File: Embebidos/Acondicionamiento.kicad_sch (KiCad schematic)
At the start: 21 parts, among them IC1 ESP32-WROVER-B__8MB_, SW1 SW_Reset, SW2 SW_Boot

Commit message: LDR_69Errores
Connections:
- net LDR_IN: now reaches IC1.7 (IO35)
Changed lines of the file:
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@@
     (effects (font (size 1.27 1.27)) (justify left))
+  )
+  (hierarchical_label "LDR_IN" (shape input) (at 114.3 83.82 180)
+    (effects (font (size 1.27 1.27)) (justify right))
   )
   (hierarchical_label "RXSIM" (shape bidirectional) (at 186.69 107.95 0)

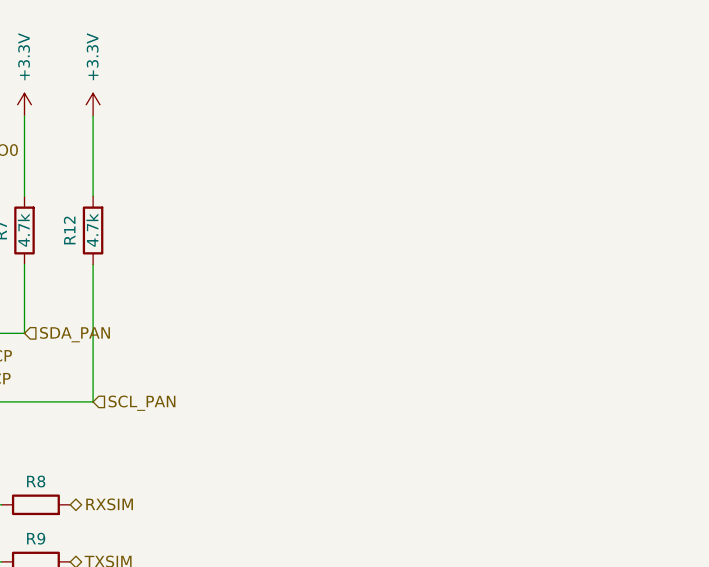
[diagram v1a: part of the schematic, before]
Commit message: conectoresRFySIM
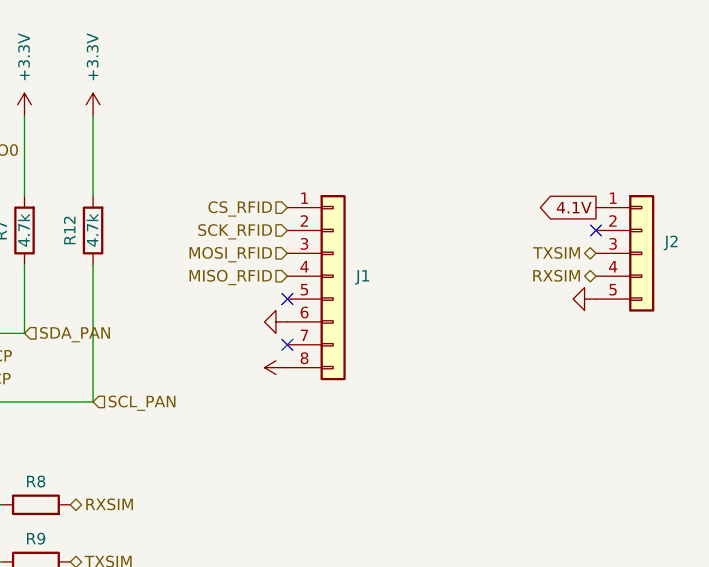
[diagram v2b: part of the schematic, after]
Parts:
- added J1: (no value), symbol Connector_Generic:Conn_01x08
- added J2: (no value), symbol Connector_Generic:Conn_01x05
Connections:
- net +3.3V: now also J1.8 (Pin_8)
- net CS_RFID: now also J1.1 (Pin_1)
- net GND: now also J1.6 (Pin_6), J2.5 (Pin_5)
- net MISO_RFID: now also J1.4 (Pin_4)
- net MOSI_RFID: now also J1.3 (Pin_3)
- net RXSIM: now also J2.4 (Pin_4)
- net SCK_RFID: now also J1.2 (Pin_2)
- net TXSIM: now also J2.3 (Pin_3)
- new net 4.1V: J2.1 (Pin_1)
- no-connect marks 19 -> 22

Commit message: Mosfet Luces
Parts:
- J1: value (none) -> Conn_01x08
- J2: value (none) -> Conn_01x05
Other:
- moved on the sheet: J1, J2
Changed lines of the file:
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@@
   (no_connect (at 152.4 76.2))
   (no_connect (at 152.4 86.36))
-  (no_connect (at 245.11 77.47))
+  (no_connect (at 251.46 24.13))
   (no_connect (at 152.4 104.14))
   (no_connect (at 152.4 114.3))
   (no_connect (at 152.4 124.46))
-  (no_connect (at 210.82 85.09))
-  (no_connect (at 210.82 90.17))
+  (no_connect (at 251.46 58.42))
+  (no_connect (at 251.46 63.5))
   (wire (pts (xy 68.58 80.01) (xy 68.58 82.55))
     (stroke (width 0) (type default) (color 0 0 0 0))
@@
     (effects (font (size 1.27 1.27)) (justify right bottom))
   )
-  (global_label "4.1V" (shape output) (at 245.11 74.93 180) (fields_autoplaced)
-    (effects (font (size 1.27 1.27)) (justify right))
-    (property "Intersheet References" "${INTERSHEET_REFS}" (id 0) (at 238.5845 74.8506 0)
+  (global_label "4.1V" (shape output) (at 251.46 21.59 180) (fields_autoplaced)
+    (effects (font (size 1.27 1.27)) (justify right))
+    (property "Intersheet References" "${INTERSHEET_REFS}" (id 0) (at 244.9345 21.5106 0)
       (effects (font (size 1.27 1.27)) (justify right) hide)
     )
@@
     (effects (font (size 1.27 1.27)) (justify right))
   )
-  (hierarchical_label "MOSI_RFID" (shape input) (at 210.82 80.01 180)
+  (hierarchical_label "MOSI_RFID" (shape input) (at 251.46 53.34 180)
     (effects (font (size 1.27 1.27)) (justify right))
   )
@@
     (effects (font (size 1.27 1.27)) (justify left))
   )
-  (hierarchical_label "TXSIM" (shape bidirectional) (at 245.11 80.01 180)
+  (hierarchical_label "TXSIM" (shape bidirectional) (at 251.46 26.67 180)
     (effects (font (size 1.27 1.27)) (justify right))
   )
@@
     (effects (font (size 1.27 1.27)) (justify right))
   )
-  (hierarchical_label "MISO_RFID" (shape input) (at 210.82 82.55 180)
+  (hierarchical_label "MISO_RFID" (shape input) (at 251.46 55.88 180)
     (effects (font (size 1.27 1.27)) (justify right))
   )
@@
     (effects (font (size 1.27 1.27)) (justify right))
   )
-  (hierarchical_label "RXSIM" (shape bidirectional) (at 245.11 82.55 180)
+  (hierarchical_label "RXSIM" (shape bidirectional) (at 251.46 29.21 180)
     (effects (font (size 1.27 1.27)) (justify right))
   )
@@
     (effects (font (size 1.27 1.27)) (justify left))
   )
-  (hierarchical_label "CS_RFID" (shape input) (at 210.82 74.93 180)
-    (effects (font (size 1.27 1.27)) (justify right))
-  )
-  (hierarchical_label "SCK_RFID" (shape input) (at 210.82 77.47 180)
+  (hierarchical_label "CS_RFID" (shape input) (at 251.46 48.26 180)
+    (effects (font (size 1.27 1.27)) (justify right))
+  )
+  (hierarchical_label "SCK_RFID" (shape input) (at 251.46 50.8 180)
     (effects (font (size 1.27 1.27)) (justify right))
   )
@@
     (effects (font (size 1.27 1.27)) (justify left))
   )
-  (symbol (lib_id "Connector_Generic:Conn_01x08") (at 215.9 82.55 0) (unit 1)
-    (in_bom yes) (on_board yes) (fields_autoplaced)
-    (property "Reference" "J1" (id 0) (at 218.44 82.5499 0)
-      (effects (font (size 1.27 1.27)) (justify left))
-    )
-    (property "Value" "" (id 1) (at 218.44 85.0899 0)
-      (effects (font (size 1.27 1.27)) (justify left))
-    )
-    (property "Footprint" "" (id 2) (at 215.9 82.55 0)
-      (effects (font (size 1.27 1.27)) hide)
-    )
-    (property "Datasheet" "~" (id 3) (at 215.9 82.55 0)
+  (symbol (lib_id "Connector_Generic:Conn_01x08") (at 256.54 55.88 0) (unit 1)
+    (in_bom yes) (on_board yes) (fields_autoplaced)
+    (property "Reference" "J1" (id 0) (at 259.08 55.8799 0)
+      (effects (font (size 1.27 1.27)) (justify left))
+    )
+    (property "Value" "Conn_01x08" (id 1) (at 259.08 58.4199 0)
+      (effects (font (size 1.27 1.27)) (justify left))
+    )
+    (property "Footprint" "" (id 2) (at 256.54 55.88 0)
+      (effects (font (size 1.27 1.27)) hide)
+    )
+    (property "Datasheet" "~" (id 3) (at 256.54 55.88 0)
       (effects (font (size 1.27 1.27)) hide)
     )
@@
     (pin "2")
   )
-  (symbol (lib_id "Connector_Generic:Conn_01x05") (at 250.19 80.01 0) (unit 1)
-    (in_bom yes) (on_board yes) (fields_autoplaced)
-    (property "Reference" "J2" (id 0) (at 252.73 78.7399 0)
-      (effects (font (size 1.27 1.27)) (justify left))
-    )
-    (property "Value" "" (id 1) (at 252.73 81.2799 0)
-      (effects (font (size 1.27 1.27)) (justify left))
-    )
-    (property "Footprint" "" (id 2) (at 250.19 80.01 0)
-      (effects (font (size 1.27 1.27)) hide)
-    )
-    (property "Datasheet" "~" (id 3) (at 250.19 80.01 0)
+  (symbol (lib_id "Connector_Generic:Conn_01x05") (at 256.54 26.67 0) (unit 1)
+    (in_bom yes) (on_board yes) (fields_autoplaced)
+    (property "Reference" "J2" (id 0) (at 259.08 25.3999 0)
+      (effects (font (size 1.27 1.27)) (justify left))
+    )
+    (property "Value" "Conn_01x05" (id 1) (at 259.08 27.9399 0)
+      (effects (font (size 1.27 1.27)) (justify left))
+    )
+    (property "Footprint" "" (id 2) (at 256.54 26.67 0)
+      (effects (font (size 1.27 1.27)) hide)
+    )
+    (property "Datasheet" "~" (id 3) (at 256.54 26.67 0)
       (effects (font (size 1.27 1.27)) hide)
     )
@@
     (pin "1")
   )
-  (symbol (lib_id "power:+3.3V") (at 210.82 92.71 90) (unit 1)
-    (in_bom yes) (on_board yes) (fields_autoplaced)
-    (property "Reference" "#PWR?" (id 0) (at 214.63 92.71 0)
-      (effects (font (size 1.27 1.27)) hide)
-    )
-    (property "Value" "" (id 1) (at 207.01 92.7099 90)
-      (effects (font (size 1.27 1.27)) (justify left))
-    )
-    (property "Footprint" "" (id 2) (at 210.82 92.71 0)
-      (effects (font (size 1.27 1.27)) hide)
-    )
-    (property "Datasheet" "" (id 3) (at 210.82 92.71 0)
+  (symbol (lib_id "power:+3.3V") (at 251.46 66.04 90) (unit 1)
+    (in_bom yes) (on_board yes) (fields_autoplaced)
+    (property "Reference" "#PWR?" (id 0) (at 255.27 66.04 0)
+      (effects (font (size 1.27 1.27)) hide)
+    )
+    (property "Value" "+3.3V" (id 1) (at 247.65 66.0399 90)
+      (effects (font (size 1.27 1.27)) (justify left))
+    )
+    (property "Footprint" "" (id 2) (at 251.46 66.04 0)
+      (effects (font (size 1.27 1.27)) hide)
+    )
+    (property "Datasheet" "" (id 3) (at 251.46 66.04 0)
       (effects (font (size 1.27 1.27)) hide)
     )
@@
     (pin "1")
   )
-  (symbol (lib_id "power:GND") (at 210.82 87.63 270) (unit 1)
-    (in_bom yes) (on_board yes) (fields_autoplaced)
-    (property "Reference" "#PWR?" (id 0) (at 204.47 87.63 0)
-      (effects (font (size 1.27 1.27)) hide)
-    )
-    (property "Value" "" (id 1) (at 207.01 87.6299 90)
+  (symbol (lib_id "power:GND") (at 251.46 60.96 270) (unit 1)
+    (in_bom yes) (on_board yes) (fields_autoplaced)
+    (property "Reference" "#PWR?" (id 0) (at 245.11 60.96 0)
+      (effects (font (size 1.27 1.27)) hide)
+    )
+    (property "Value" "GND" (id 1) (at 247.65 60.9599 90)
       (effects (font (size 1.27 1.27)) (justify right))
     )
-    (property "Footprint" "" (id 2) (at 210.82 87.63 0)
-      (effects (font (size 1.27 1.27)) hide)
-    )
-    (property "Datasheet" "" (id 3) (at 210.82 87.63 0)
+    (property "Footprint" "" (id 2) (at 251.46 60.96 0)
+      (effects (font (size 1.27 1.27)) hide)
+    )
+    (property "Datasheet" "" (id 3) (at 251.46 60.96 0)
       (effects (font (size 1.27 1.27)) hide)
     )
@@
     (pin "1")
   )
-  (symbol (lib_id "power:GND") (at 245.11 85.09 270) (unit 1)
-    (in_bom yes) (on_board yes) (fields_autoplaced)
-    (property "Reference" "#PWR?" (id 0) (at 238.76 85.09 0)
-      (effects (font (size 1.27 1.27)) hide)
-    )
-    (property "Value" "" (id 1) (at 241.3 85.0899 90)
+  (symbol (lib_id "power:GND") (at 251.46 31.75 270) (unit 1)
+    (in_bom yes) (on_board yes) (fields_autoplaced)
+    (property "Reference" "#PWR?" (id 0) (at 245.11 31.75 0)
+      (effects (font (size 1.27 1.27)) hide)
+    )
+    (property "Value" "GND" (id 1) (at 247.65 31.7499 90)
       (effects (font (size 1.27 1.27)) (justify right))
     )
-    (property "Footprint" "" (id 2) (at 245.11 85.09 0)
-      (effects (font (size 1.27 1.27)) hide)
-    )
-    (property "Datasheet" "" (id 3) (at 245.11 85.09 0)
-      (effects (font (size 1.27 1.27)) hide)
-    )
+    (property "Footprint" "" (id 2) (at 251.46 31.75 0)
+      (effects (font (size 1.27 1.27)) hide)
+    )
+    (property "Datasheet" "" (id 3) (at 251.46 31.75 0)
+      (effects (font (size 1.27 1.27)) hide)
+    )

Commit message: COnecxion
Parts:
- R1: value ~ -> 470
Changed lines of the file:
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@@
     (in_bom yes) (on_board yes)
     (property "Reference" "R1" (id 0) (at 59.69 78.74 90))
-    (property "Value" "~" (id 1) (at 57.15 78.74 90))
+    (property "Value" "470" (id 1) (at 57.15 78.74 90))
     (property "Footprint" "" (id 2) (at 55.372 78.74 90)
       (effects (font (size 1.27 1.27)) hide)

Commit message: transistores traseros
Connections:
- net CTR 5V Inf: no longer names the net of IC1.14 (IO12)
- net CTR 5V LEDS renamed ctr_trasero
- net CTR_LED_delantero renamed ctr_led_delantero
- no-connect marks 22 -> 23
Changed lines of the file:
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@@
   (no_connect (at 152.4 119.38))
   (no_connect (at 152.4 106.68))
+  (no_connect (at 114.3 101.6))
   (no_connect (at 152.4 73.66))
   (no_connect (at 152.4 76.2))
@@
     (effects (font (size 1.27 1.27)) (justify left))
   )
-  (hierarchical_label "CTR 5V LEDS" (shape output) (at 152.4 71.12 0)
+  (hierarchical_label "ctr_trasero" (shape output) (at 152.4 71.12 0)
     (effects (font (size 1.27 1.27)) (justify left))
   )
@@
     (effects (font (size 1.27 1.27)) (justify left))
   )
-  (hierarchical_label "CTR_LED_delantero" (shape output) (at 114.3 127 180)
+  (hierarchical_label "ctr_led_delantero" (shape output) (at 114.3 127 180)
     (effects (font (size 1.27 1.27)) (justify right))
   )
@@
     (effects (font (size 1.27 1.27)) (justify right))
   )
-  (hierarchical_label "CTR 5V Inf" (shape output) (at 114.3 101.6 180)
-    (effects (font (size 1.27 1.27)) (justify right))
-  )

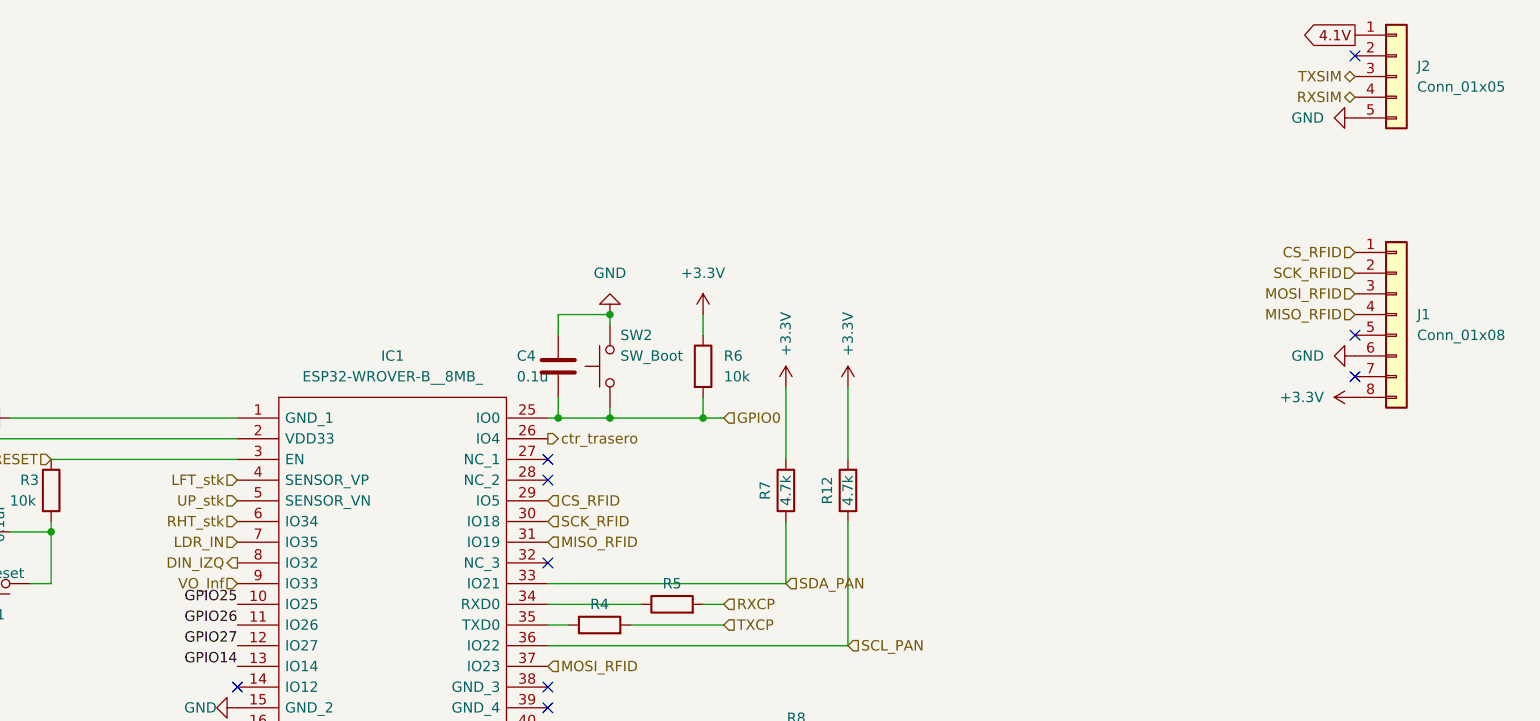
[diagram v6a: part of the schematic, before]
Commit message: Cambio de anotacion y Vcc ldr
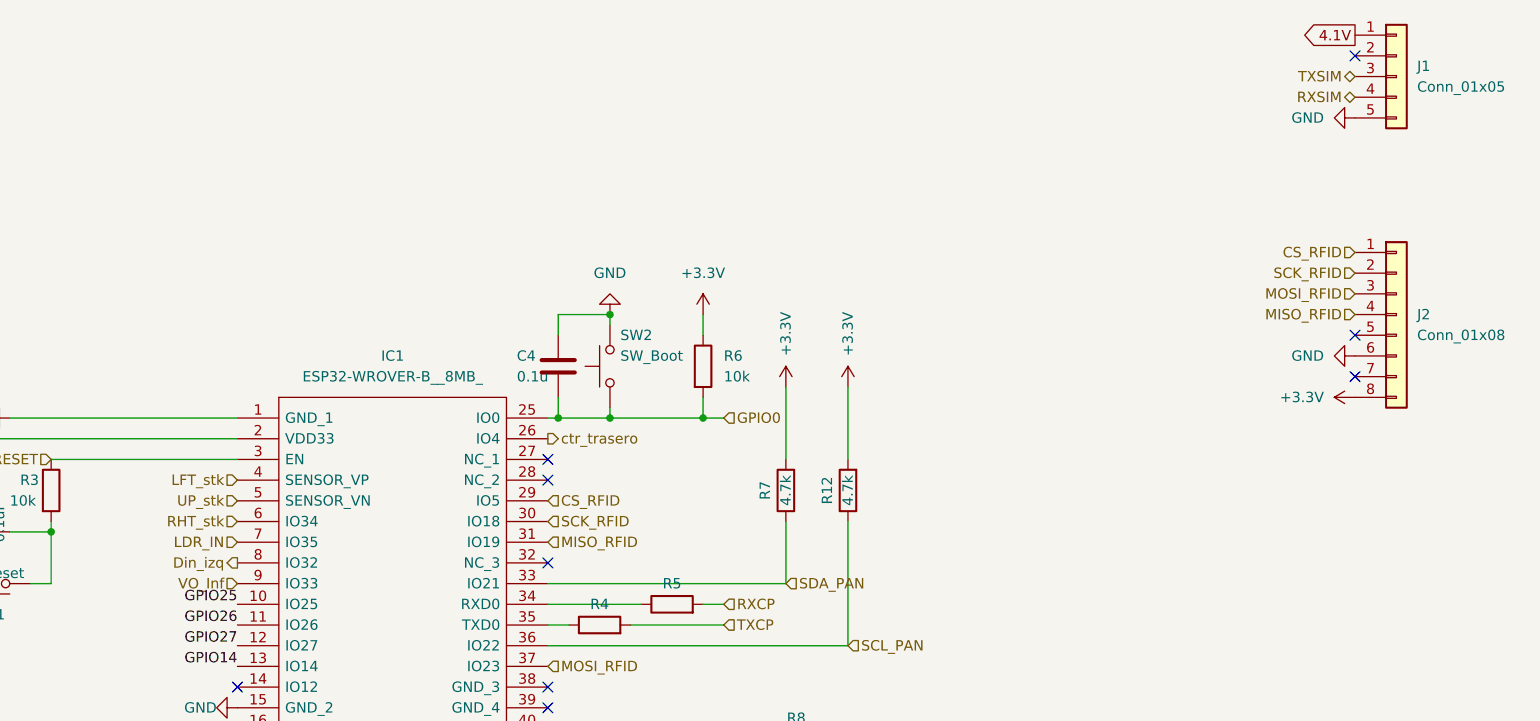
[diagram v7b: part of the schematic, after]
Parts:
- renumbered J2 to J1, J1 to J2
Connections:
- net DIN_IZQ renamed Din_izq
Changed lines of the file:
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@@
     (effects (font (size 1.27 1.27)) (justify right))
   )
-  (hierarchical_label "DIN_IZQ" (shape output) (at 114.3 86.36 180)
+  (hierarchical_label "Din_izq" (shape output) (at 114.3 86.36 180)
     (effects (font (size 1.27 1.27)) (justify right))
   )
@@
   (symbol (lib_id "Connector_Generic:Conn_01x08") (at 256.54 55.88 0) (unit 1)
     (in_bom yes) (on_board yes) (fields_autoplaced)
-    (property "Reference" "J1" (id 0) (at 259.08 55.8799 0)
+    (property "Reference" "J2" (id 0) (at 259.08 55.8799 0)
       (effects (font (size 1.27 1.27)) (justify left))
     )
@@
   (symbol (lib_id "Connector_Generic:Conn_01x05") (at 256.54 26.67 0) (unit 1)
     (in_bom yes) (on_board yes) (fields_autoplaced)
-    (property "Reference" "J2" (id 0) (at 259.08 25.3999 0)
+    (property "Reference" "J1" (id 0) (at 259.08 25.3999 0)
       (effects (font (size 1.27 1.27)) (justify left))
     )
@@
   (symbol (lib_id "power:+3.3V") (at 251.46 66.04 90) (unit 1)
     (in_bom yes) (on_board yes) (fields_autoplaced)
-    (property "Reference" "#PWR0102" (id 0) (at 255.27 66.04 0)
+    (property "Reference" "#PWR013" (id 0) (at 255.27 66.04 0)
       (effects (font (size 1.27 1.27)) hide)
     )
@@
   (symbol (lib_id "power:GND") (at 251.46 60.96 270) (unit 1)
     (in_bom yes) (on_board yes) (fields_autoplaced)
-    (property "Reference" "#PWR0103" (id 0) (at 245.11 60.96 0)
+    (property "Reference" "#PWR012" (id 0) (at 245.11 60.96 0)
       (effects (font (size 1.27 1.27)) hide)
     )
@@
   (symbol (lib_id "power:GND") (at 251.46 31.75 270) (unit 1)
     (in_bom yes) (on_board yes) (fields_autoplaced)
-    (property "Reference" "#PWR0101" (id 0) (at 245.11 31.75 0)
-      (effects (font (size 1.27 1.27)) hide)
-    )
+    (property "Reference" "#PWR011" (id 0) (at 245.11 31.75 0)
+      (effects (font (size 1.27 1.27)) hide)
+    )
